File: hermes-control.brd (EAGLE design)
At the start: 106 x 47 mm, 76 parts, among them J1 1981568-1, J3 2201778-1, Q1 MMBT2222A, Q2 BC849SMD, Q3 FDN360P, Q4 FDN360P, Q5 BC849SMD, Q6 MMBT3906SOT23-3, Q7 FDN360P, Q8 MMBT2222A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

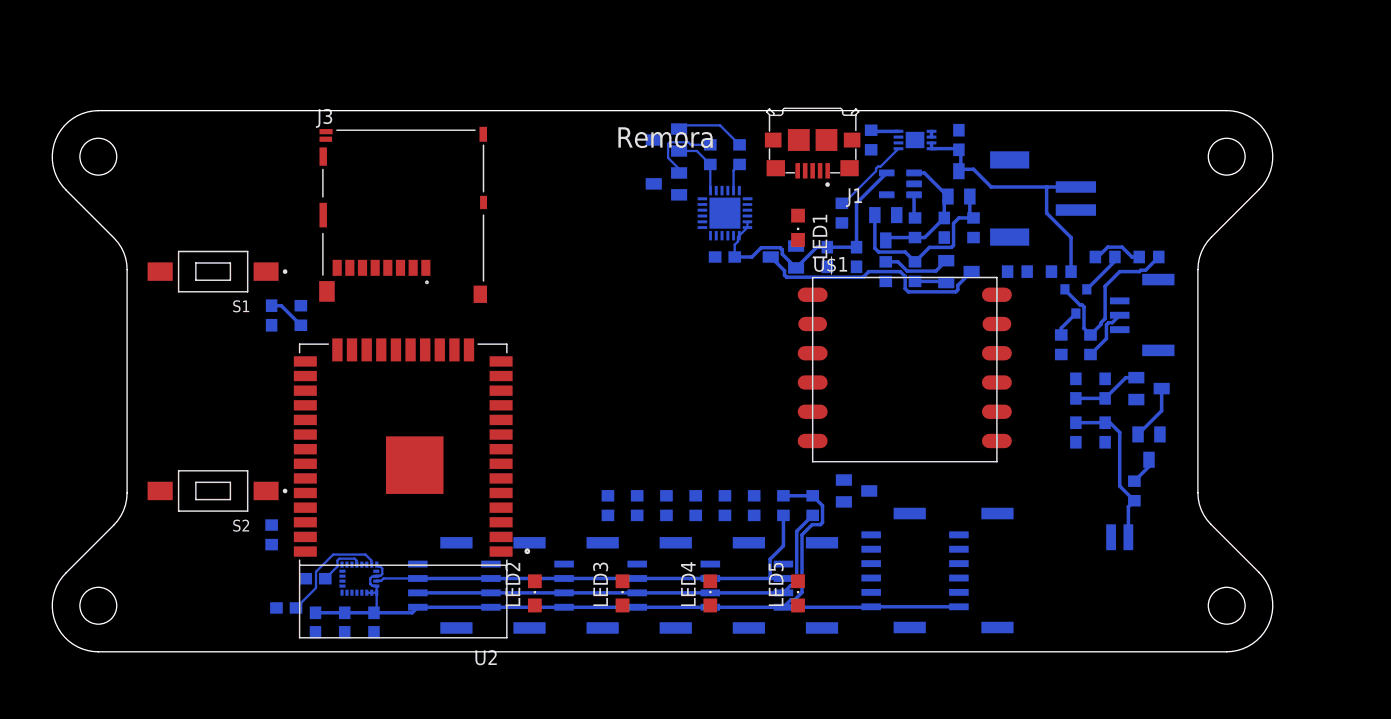
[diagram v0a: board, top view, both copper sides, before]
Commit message: ripped up all signal
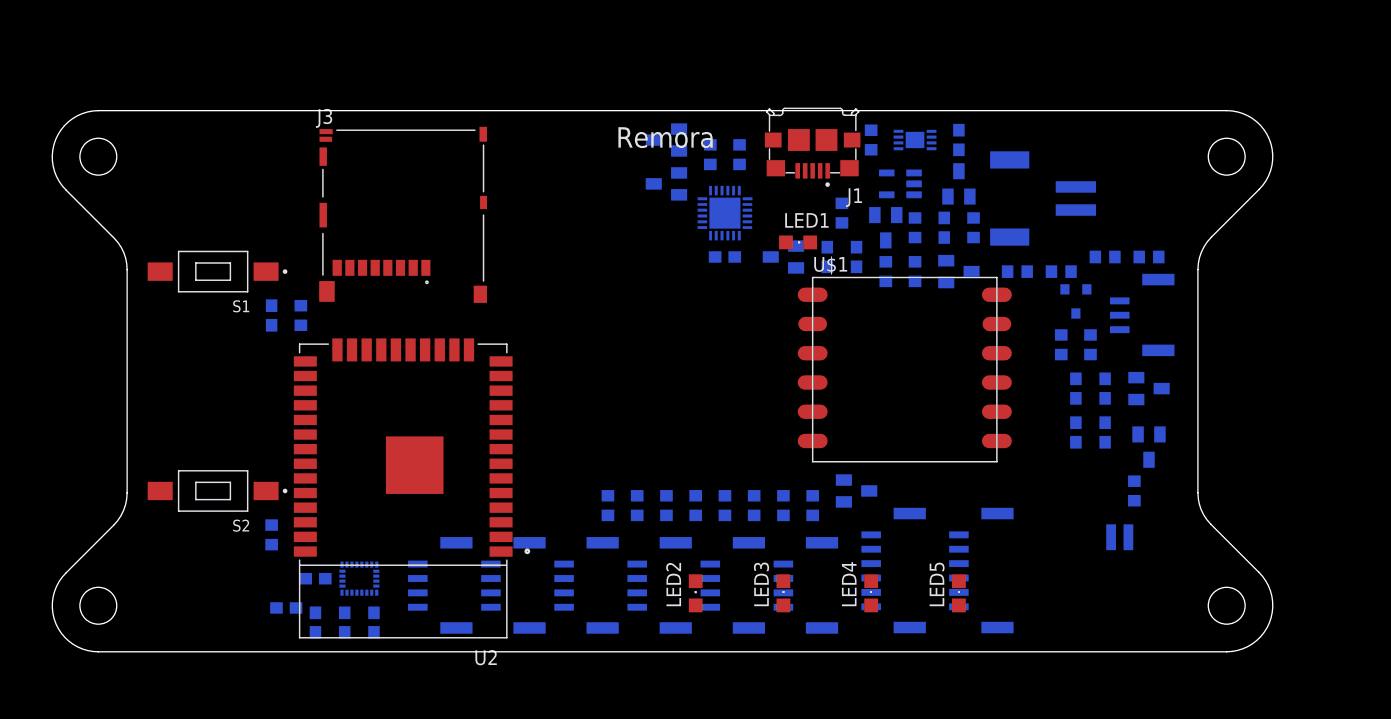
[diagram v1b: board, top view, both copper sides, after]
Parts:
- moved LED2 14.0 mm to (55.9, 5.08)
- moved LED4 14.0 mm to (71.1, 5.08)
- moved LED3 14.0 mm to (63.5, 5.08)
- moved LED5 14.0 mm to (78.7, 5.08)
- moved LED1 1.27 mm to (64.8, 35.6), turned to 270 degrees
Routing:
- net 3.3V: track 108.0 -> 0.00 mm
- net SDA: track 41.5 -> 0.00 mm
- net SCL: track 39.7 -> 0.00 mm
- net V_BATT: track 23.8 -> 0.00 mm
- net VCCIO: track 23.7 -> 0.00 mm
- net VCC: track 17.1 -> 0.00 mm
- net N$13: track 15.5 -> 0.00 mm
- net N$15: track 14.0 -> 0.00 mm
- net N$4: track 11.7 -> 0.00 mm
- net N$10: track 9.87 -> 0.00 mm
- net N$2: track 7.01 -> 0.00 mm
- net N$20: track 6.73 -> 0.00 mm
- net N$19: track 6.08 -> 0.00 mm
- net N$6: track 6.00 -> 0.00 mm
- net VCC_SENSE: track 5.96 -> 0.00 mm
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
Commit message: almost everything is connected
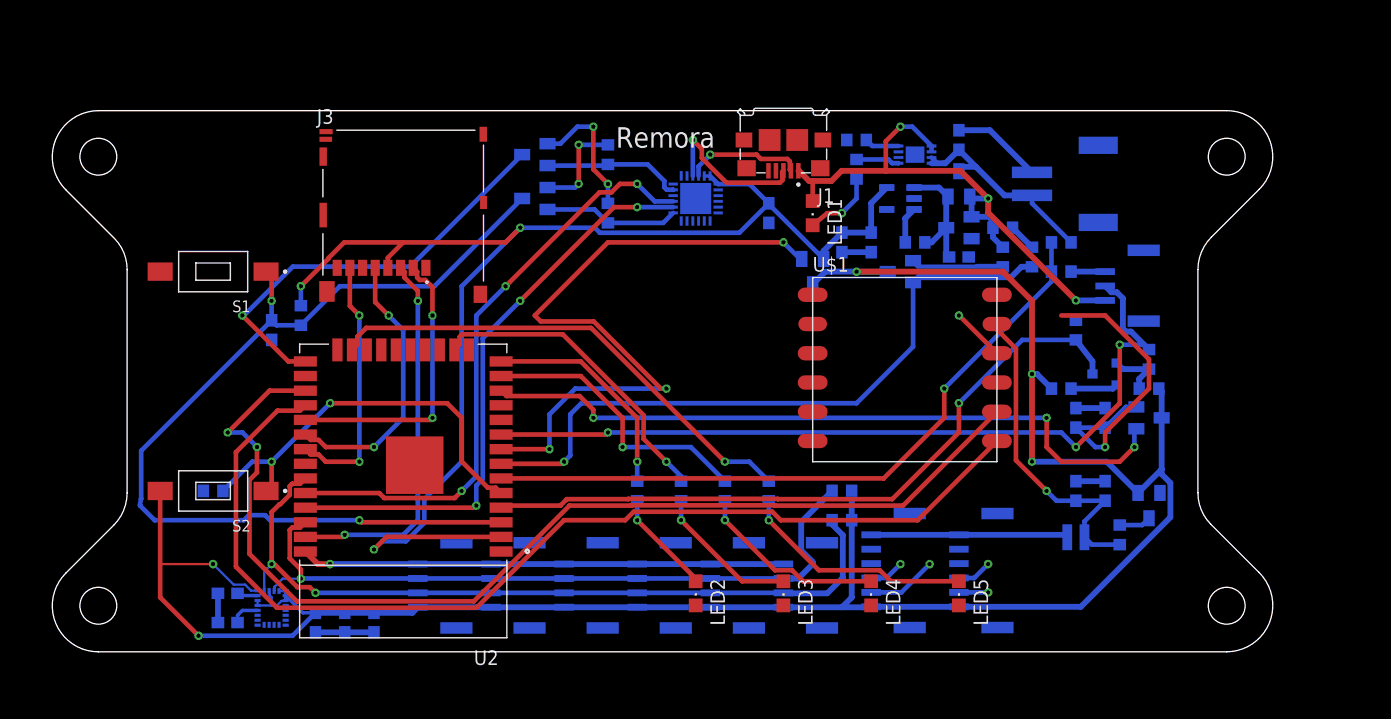
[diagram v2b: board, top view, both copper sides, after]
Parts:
- removed Q1: MMBT2222A, hermes:SOT23
- removed R11, R5: 4.7k, rcl:R0603
- moved R9 12.8 mm to (85.1, 34.3), turned to 270 degrees
- moved Q2 12.5 mm to (41.9, 39.4)
- moved R12 12.0 mm to (87.6, 22.9)
- moved Q5 11.7 mm to (41.9, 43.2)
- moved R10 11.4 mm to (48.3, 43.2)
- moved R13 11.4 mm to (95.2, 22.9), turned to 180 degrees
- moved R21 10.2 mm to (48.3, 38.1)
- moved C9 8.52 mm to (15.2, 2.54)
- moved U1 8.03 mm to (19.1, 3.81), turned to 270 degrees
- moved R25 7.73 mm to (82.5, 34.3)
- moved Q6 6.84 mm to (91.4, 24.1), turned to 270 degrees
- moved R18 6.48 mm to (62.2, 14.0)
- moved R8 6.35 mm to (14.0, 14.0), turned to 180 degrees
- moved D1 6.35 mm to (78.7, 36.8), turned to 270 degrees
- moved C6 5.39 mm to (62.2, 38.1), turned to 270 degrees
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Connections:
- removed net GPSRESET: R11.1
- removed net N$12: Q1.3, U$1.10
- removed net N$8: Q1.1, R11.2, R5.1
- net 3.3V: no longer J3.4
- net GND: no longer Q1.2, R5.2
- net VCCIO: now also J3.4
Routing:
- net 3.3V: track 0.00 -> 195.8 mm, vias 0 -> 5
- net VCCIO: track 0.00 -> 117.7 mm, vias 0 -> 3
- net RX1: track 0.00 -> 94.3 mm, vias 0 -> 2
- net TX1: track 0.00 -> 91.8 mm
- net GND: track 0.00 -> 87.5 mm, vias 0 -> 1
- net ESP_RST: track 0.00 -> 84.0 mm, vias 0 -> 2
- net PROBE: track 0.00 -> 71.4 mm, vias 0 -> 3
- net SCL: track 0.00 -> 68.3 mm, vias 0 -> 2
- net SDA: track 0.00 -> 62.1 mm, vias 0 -> 1
- net GPS_EN: track 0.00 -> 61.6 mm, vias 0 -> 3
- net WATER: track 0.00 -> 60.9 mm, vias 0 -> 1
- net IO13: track 0.00 -> 59.8 mm, vias 0 -> 1
- net 3.3_EN: track 0.00 -> 58.8 mm, vias 0 -> 3
- net VCC_SENSE: track 0.00 -> 58.6 mm, vias 0 -> 1
- net RX0: track 0.00 -> 52.2 mm, vias 0 -> 3
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
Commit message: all connections made
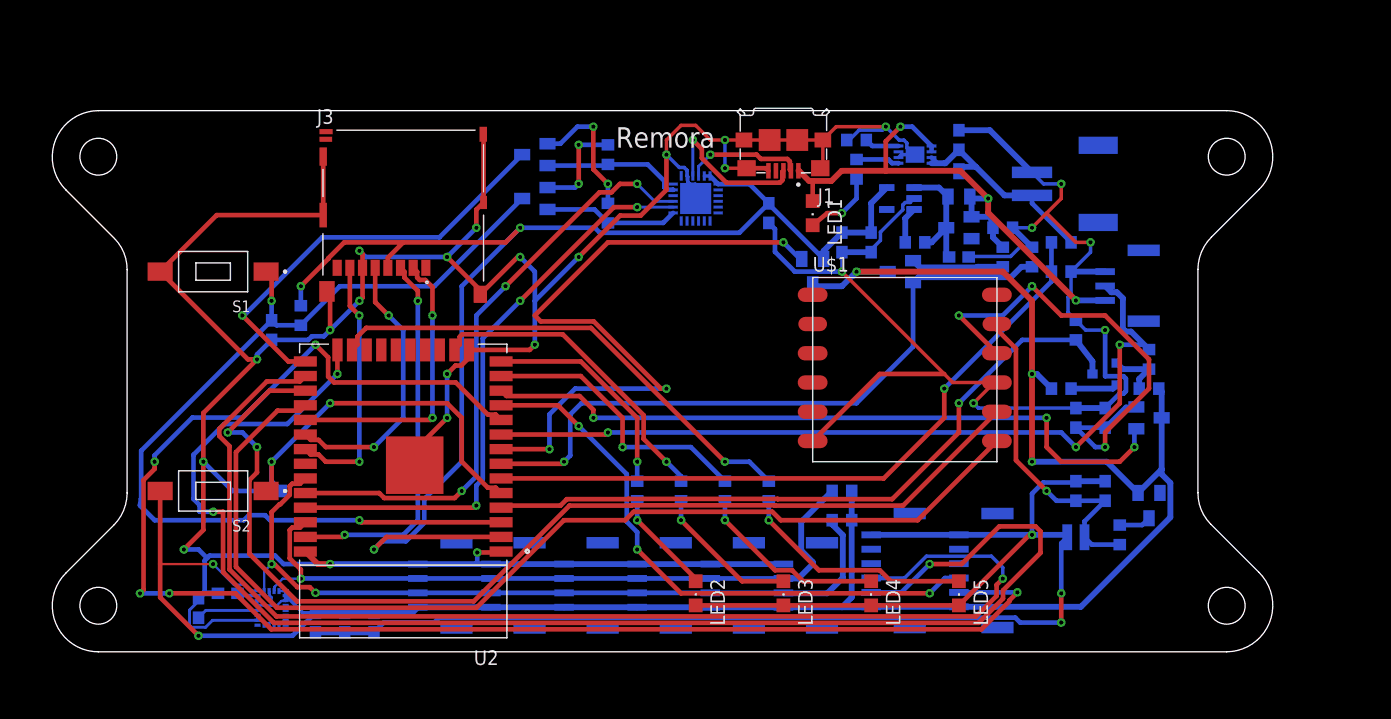
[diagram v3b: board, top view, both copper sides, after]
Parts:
- moved R8 5.08 mm to (19.1, 14.0)
- moved C9 2.84 mm to (12.7, 3.81), turned to 90 degrees
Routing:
- net GND: track 87.5 -> 521.6 mm, vias 1 -> 28
- net TX3: track 2.54 -> 134.2 mm, vias 1 -> 5
- net TX2: track 6.10 -> 124.8 mm, vias 1 -> 3
- net RX2: track 3.04 -> 106.3 mm
- net RX3: track 3.04 -> 50.4 mm, vias 1 -> 3
- net N$6: track 32.3 -> 43.3 mm, vias 2 -> 3
- net N$9: track 2.55 -> 5.39 mm
- net CONFIG: track 35.5 -> 33.1 mm

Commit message: added gnd plane
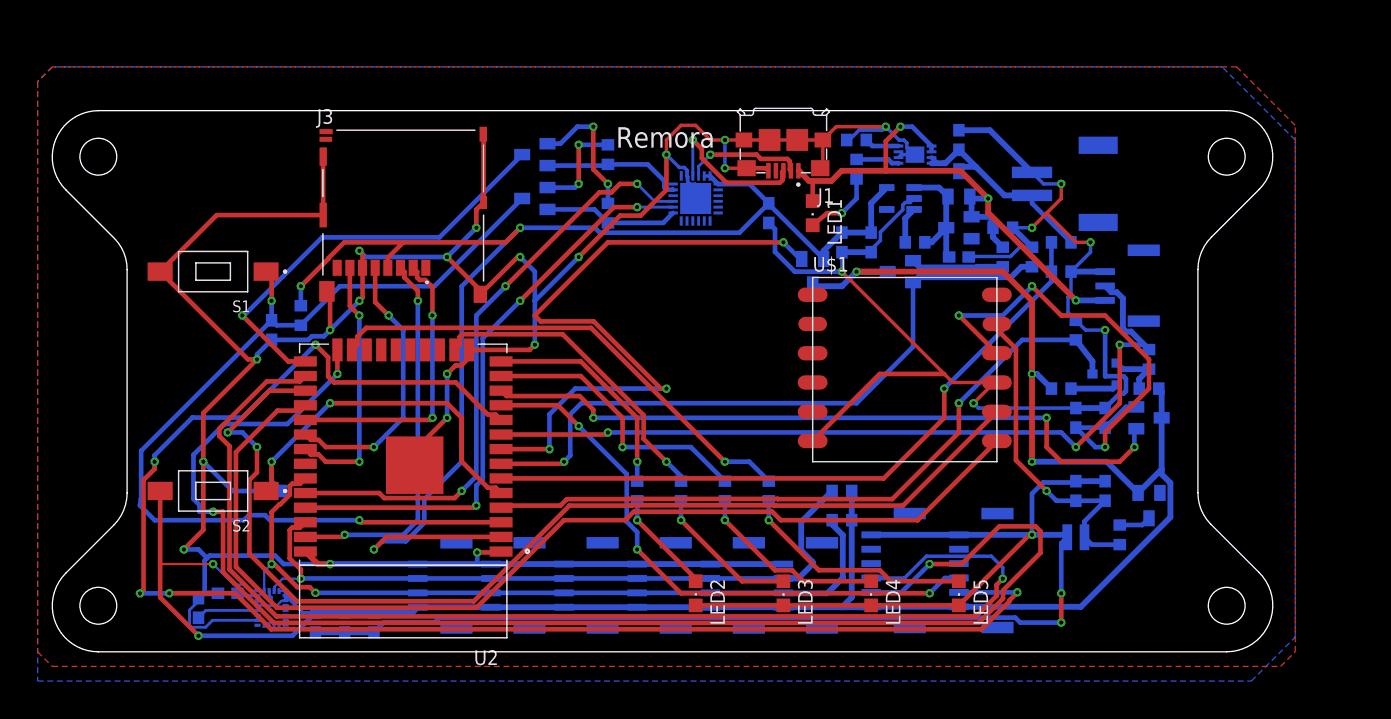
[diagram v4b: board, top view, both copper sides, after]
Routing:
- added copper zone on layer 1, net GND
- added copper zone on layer 16, net GND
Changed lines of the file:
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@@
 <wire x1="27.94" y1="1.69" x2="28.79" y2="2.54" width="0.4064" layer="16"/>
 <via x="87.63" y="2.54" extent="1-16" drill="0.35"/>
-<wire x1="28.79" y1="2.54" x2="33.16710625" y2="2.54" width="0.4064" layer="16"/>
+<wire x1="28.79" y1="2.54" x2="30.48" y2="2.54" width="0.4064" layer="16"/>
+<wire x1="30.48" y1="2.54" x2="33.16710625" y2="2.54" width="0.4064" layer="16"/>
 <wire x1="84.06289375" y1="2.54" x2="87.63" y2="2.54" width="0.4064" layer="16"/>
 <wire x1="83.63729375" y1="2.9656" x2="84.06289375" y2="2.54" width="0.4064" layer="16"/>
@@
 <wire x1="51.10395" y1="37.8862" x2="53.34" y2="40.12225" width="0.4064" layer="1"/>
 <wire x1="53.34" y1="40.12225" x2="53.34" y2="43.18" width="0.4064" layer="1"/>
-<wire x1="73.495" y1="42.93" x2="74.845" y2="39.37" width="0" layer="19" extent="16-16"/>
-<wire x1="63.5" y1="4.03" x2="63.5" y2="7.62" width="0" layer="19" extent="1-16"/>
+<polygon width="0.4064" layer="1">
+<vertex x="-1.27" y="49.53"/>
+<vertex x="-1.27" y="0"/>
+<vertex x="0" y="-1.27"/>
+<vertex x="106.68" y="-1.27"/>
+<vertex x="107.95" y="0"/>
+<vertex x="107.95" y="45.72"/>
+<vertex x="102.87" y="50.8"/>
+<vertex x="0" y="50.8"/>
+</polygon>
+<polygon width="0.4064" layer="16">
+<vertex x="-1.27" y="49.53"/>
+<vertex x="-1.27" y="-2.54"/>
+<vertex x="104.14" y="-2.54"/>
+<vertex x="107.95" y="1.27"/>
+<vertex x="107.95" y="44.45"/>
+<vertex x="101.6" y="50.8"/>
+<vertex x="0" y="50.8"/>
+</polygon>
 </signal>
 <signal name="3.3V">

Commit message: fixed air wires and isolated 0.1
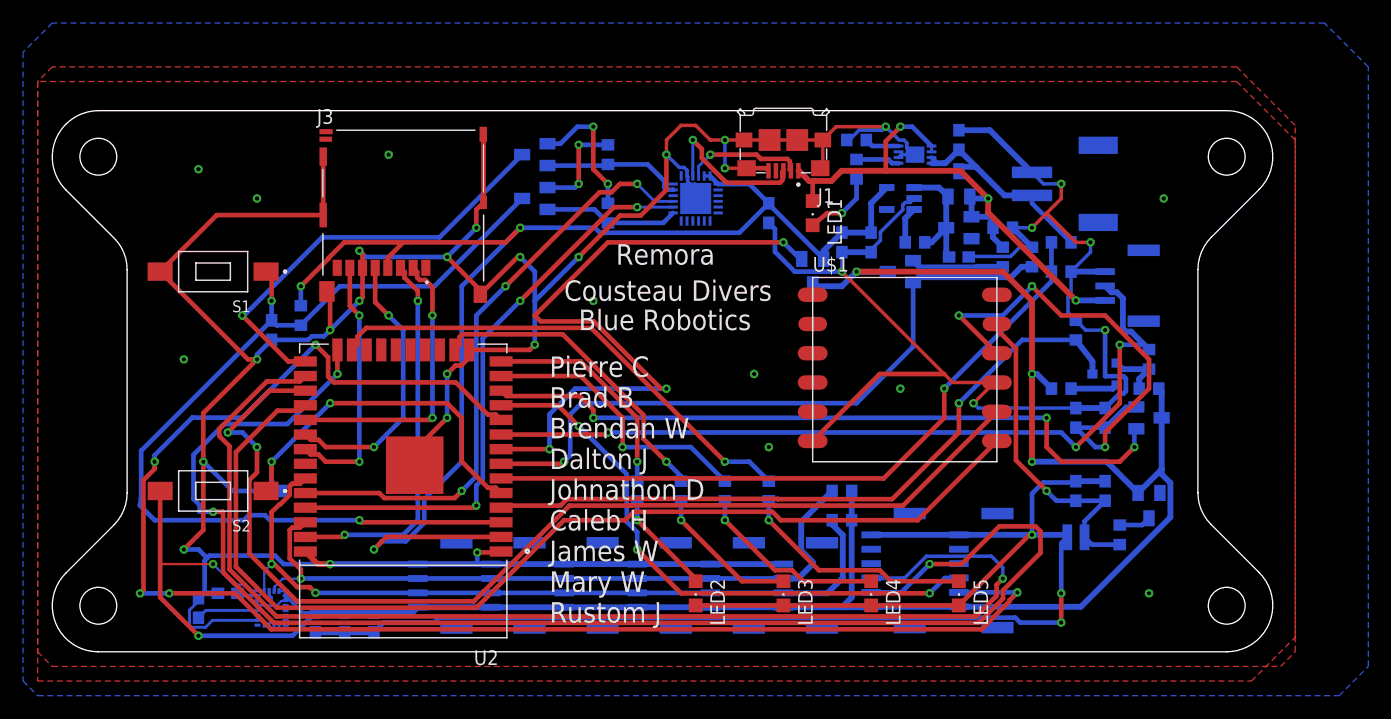
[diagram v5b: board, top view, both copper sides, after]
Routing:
- net GND: vias 28 -> 29
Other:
- board text added: "Blue Robotics"
- board text added: "Cousteau Divers"
- board text added: "Pierre C Brad B Brendan W Dalton J Johnathon D Caleb H James W Mary W Rustom J"
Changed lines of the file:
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@@
 <setting verticaltext="up"/>
 </settings>
-<grid distance="50" unitdist="mil" unit="mil" style="lines" multiple="1" display="yes" altdistance="5" altunitdist="mil" altunit="mil"/>
+<grid distance="50" unitdist="mil" unit="mm" style="lines" multiple="1" display="yes" altdistance="5" altunitdist="mil" altunit="mm"/>
 <layers>
 <layer number="1" name="Top" color="4" fill="1" visible="yes" active="yes"/>
@@
 <layer number="23" name="tOrigins" color="15" fill="1" visible="yes" active="yes"/>
 <layer number="24" name="bOrigins" color="15" fill="1" visible="yes" active="yes"/>
-<layer number="25" name="tNames" color="7" fill="1" visible="yes" active="yes"/>
-<layer number="26" name="bNames" color="7" fill="1" visible="yes" active="yes"/>
+<layer number="25" name="tNames" color="7" fill="1" visible="no" active="yes"/>
+<layer number="26" name="bNames" color="7" fill="1" visible="no" active="yes"/>
 <layer number="27" name="tValues" color="7" fill="1" visible="yes" active="yes"/>
 <layer number="28" name="bValues" color="7" fill="1" visible="no" active="yes"/>
@@
 <board>
 <plain>
-<text x="53.254" y="44.673" size="1.778" layer="21" rot="R180" align="center">Remora</text>
+<text x="53.254" y="34.513" size="1.778" layer="21" rot="R180" align="center">Remora</text>
 <wire x1="1.2" y1="40.101" x2="5.4" y2="35.901" width="0.001" layer="20"/>
 <wire x1="102" y1="47.001" x2="4" y2="47.001" width="0.001" layer="20"/>
@@
 <hole x="102" y="43.001" drill="3.2"/>
 <hole x="102" y="4.001" drill="3.2"/>
+<text x="43.18" y="2.54" size="1.778" layer="21">Pierre C
+Brad B
+Brendan W
+Dalton J
+Johnathon D
+Caleb H
+James W
+Mary W
+Rustom J</text>
+<text x="44.45" y="30.48" size="1.778" layer="21">Cousteau Divers</text>
+<text x="45.72" y="27.94" size="1.778" layer="21">Blue Robotics</text>
 </plain>
 <attributes>
@@
 <vertex x="0" y="50.8"/>
 </polygon>
-<polygon width="0.4064" layer="16">
+<polygon width="0.4064" layer="1" isolate="0.1">
 <vertex x="-1.27" y="49.53"/>
 <vertex x="-1.27" y="-2.54"/>
@@
 <vertex x="107.95" y="1.27"/>
 <vertex x="107.95" y="44.45"/>
-<vertex x="101.6" y="50.8"/>
-<vertex x="0" y="50.8"/>
+<vertex x="102.87" y="49.53"/>
+</polygon>
+<via x="17.78" y="39.37" extent="1-16" drill="0.35"/>
+<polygon width="0.254" layer="16">
+<vertex x="-2.54" y="52.07"/>
+<vertex x="-2.54" y="-2.54"/>
+<vertex x="-1.27" y="-3.81"/>
+<vertex x="111.76" y="-3.81"/>
+<vertex x="114.3" y="-1.27"/>
+<vertex x="114.3" y="50.8"/>
+<vertex x="110.49" y="54.61"/>
+<vertex x="0" y="54.61"/>
 </polygon>
 </signal>
@@
 <wire x1="73.66" y1="45.6063" x2="72.39" y2="44.3363" width="0.4064" layer="1"/>
 <wire x1="72.39" y1="44.3363" x2="72.39" y2="41.775" width="0.4064" layer="1"/>
-<wire x1="76.365" y1="43.93" x2="76.365" y2="43.4888" width="0.4064" layer="16"/>
 <wire x1="79.69" y1="39.54" x2="79.84" y2="39.39" width="0.508" layer="16"/>
 <wire x1="79.84" y1="39.39" x2="79.84" y2="37.78" width="0.508" layer="16"/>
@@
 <wire x1="88.9" y1="30.52" x2="81.28" y2="38.14" width="0.508" layer="1"/>
 <wire x1="81.28" y1="38.14" x2="81.28" y2="39.37" width="0.508" layer="1"/>
-<wire x1="76.365" y1="43.4888" x2="76.365" y2="43.43" width="0" layer="19" extent="16-16"/>
+<wire x1="76.365" y1="43.93" x2="76.365" y2="43.43" width="0.254" layer="16"/>
 </signal>
 <signal name="N$2">
@@
 <wire x1="75.3464" y1="33.3836" x2="74.76" y2="33.97" width="0.508" layer="16"/>
 </signal>
+<signal name="GND1">
+<via x="12.7" y="41.91" extent="1-16" drill="0.35"/>
+</signal>
+<signal name="GND2">
+<via x="46.99" y="30.48" extent="1-16" drill="0.35"/>
+</signal>
+<signal name="GND3">
+<via x="29.21" y="43.18" extent="1-16" drill="0.35"/>
+</signal>
+<signal name="GND4">
+<via x="73.66" y="22.86" extent="1-16" drill="0.35"/>
+</signal>
+<signal name="GND5">
+<via x="96.52" y="39.37" extent="1-16" drill="0.35"/>
+</signal>
+<signal name="GND6">
+<via x="95.25" y="5.08" extent="1-16" drill="0.35"/>
+</signal>
+<signal name="GND7">
+<via x="11.43" y="25.4" extent="1-16" drill="0.35"/>
+</signal>
+<signal name="GND8">
+<via x="60.96" y="24.13" extent="1-16" drill="0.35"/>
+</signal>
+<signal name="GND9">
+<via x="62.23" y="17.78" extent="1-16" drill="0.35"/>
+</signal>
 </signals>
 <mfgpreviewcolors>
@@
 </drawing>
 <compatibility>
+<note version="6.3" minversion="6.2.2" severity="warning">
+Since Version 6.2.2 text objects can contain more than one line,
+which will not be processed correctly with this version.
+</note>
 <note version="8.2" severity="warning">
 Since Version 8.2, EAGLE supports online libraries. The ids
